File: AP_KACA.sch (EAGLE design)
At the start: 53 parts, among them IC1 REG710XX-3.3, J1 FTDI_DEVICE, M1 WIRELESS-NRF24L01, Q1 BSS123, Q2 BSS123, Q3 BSS123, Q4 BSS123, U2 MPU-6000QFN-24, U3 GY-521MPU6050, Y1 8MHz

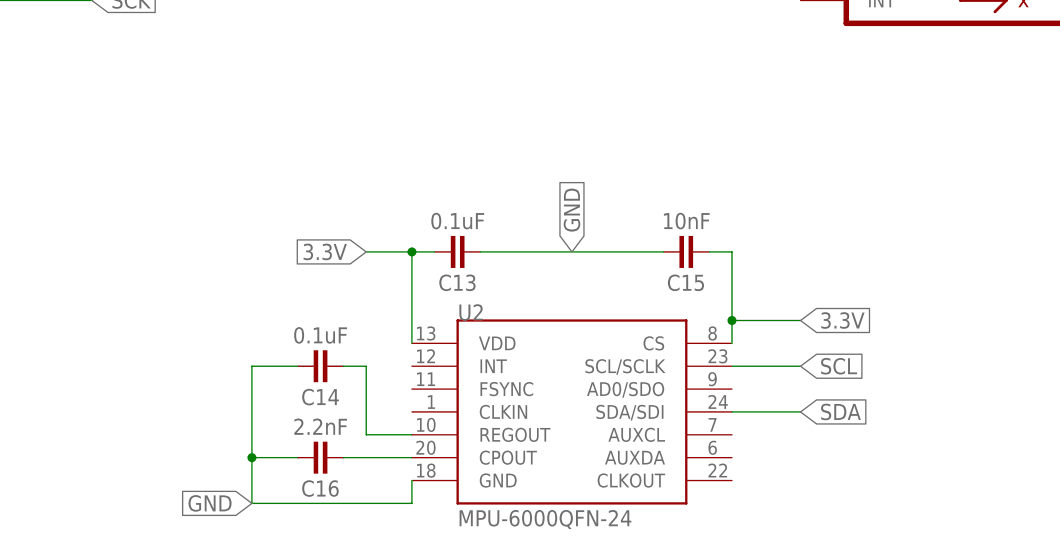
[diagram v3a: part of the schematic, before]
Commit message: removed something
removed the other imu
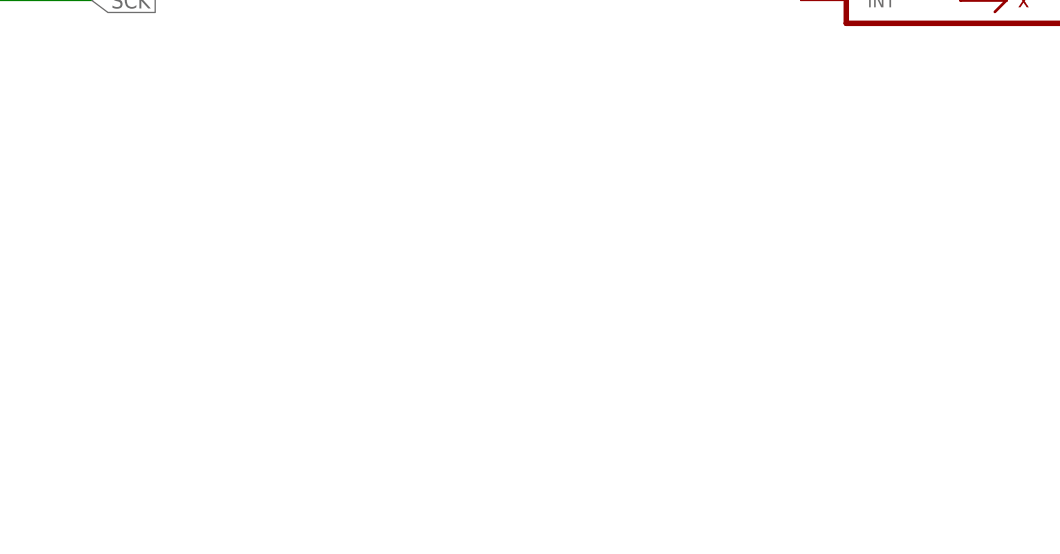
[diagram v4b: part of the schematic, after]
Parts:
- removed C13, C14: 0.1uF, we-rcl:CAPACITOR-1206
- removed C15: 10nF, we-rcl:CAPACITOR-1206
- removed C16: 2.2nF, we-rcl:CAPACITOR-1206
- removed U2: MPU-6000QFN-24, SparkFun-Sensors:MPU-6000QFN-24
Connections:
- removed net N$13: C14.1, U2.REGOUT
- removed net N$14: C16.1, U2.CPOUT
- net 3.3V: no longer C13.2, C15.1, U2.CS, U2.VDD
- net GND: no longer C13.1, C14.2, C15.2, C16.2, U2.GND
- net SCL: no longer U2.SCL/SCLK
- net SDA: no longer U2.SDA/SDI
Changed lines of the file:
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@@
 <layer number="60" name="bCarbon" color="7" fill="1" visible="no" active="no"/>
 <layer number="88" name="SimResults" color="9" fill="1" visible="yes" active="yes"/>
-<layer number="89" name="SimProbes" color="9" fill="1" visible="yes" active="yes"/>
+<layer number="89" name="SimProbes" color="9" fill="1" visible="no" active="yes"/>
 <layer number="90" name="Modules" color="5" fill="1" visible="yes" active="yes"/>
 <layer number="91" name="Nets" color="2" fill="1" visible="yes" active="yes"/>
 <layer number="92" name="Busses" color="1" fill="1" visible="yes" active="yes"/>
-<layer number="93" name="Pins" color="2" fill="1" visible="no" active="yes"/>
+<layer number="93" name="Pins" color="2" fill="1" visible="yes" active="yes"/>
 <layer number="94" name="Symbols" color="4" fill="1" visible="yes" active="yes"/>
 <layer number="95" name="Names" color="7" fill="1" visible="yes" active="yes"/>
@@
 <part name="C11" library="we-rcl" deviceset="CAPACITOR" device="-1206" value="2.2uF"/>
 <part name="C12" library="we-rcl" deviceset="CAPACITOR" device="-1206" value="2.2uF"/>
-<part name="U2" library="SparkFun-Sensors" deviceset="MPU-6000" device="QFN-24"/>
-<part name="C13" library="we-rcl" deviceset="CAPACITOR" device="-1206" value="0.1uF"/>
-<part name="C14" library="we-rcl" deviceset="CAPACITOR" device="-1206" value="0.1uF"/>
-<part name="C15" library="we-rcl" deviceset="CAPACITOR" device="-1206" value="10nF"/>
-<part name="C16" library="we-rcl" deviceset="CAPACITOR" device="-1206" value="2.2nF"/>
 <part name="R3" library="SparkFun-Resistors" deviceset="10.5KOHM1/10W1%(0603)" device="" value="36k"/>
 <part name="Q2" library="transistor-small-signal" library_urn="urn:adsk.eagle:library:401" deviceset="BSS123" device="" package3d_urn="urn:adsk.eagle:package:29752/1"/>
@@
 <instance part="C11" gate="C" x="269.24" y="48.26" rot="R180"/>
 <instance part="C12" gate="C" x="228.6" y="48.26" rot="R180"/>
-<instance part="U2" gate="G$1" x="142.24" y="-27.94"/>
-<instance part="C13" gate="C" x="129.54" y="-10.16" rot="R180"/>
-<instance part="C14" gate="C" x="114.3" y="-22.86" rot="R180"/>
-<instance part="C15" gate="C" x="154.94" y="-10.16" rot="R180"/>
-<instance part="C16" gate="C" x="114.3" y="-33.02" rot="R180"/>
 <instance part="R3" gate="G$1" x="-40.64" y="73.66" rot="R90"/>
 <instance part="Q2" gate="G$1" x="-91.44" y="83.82"/>
@@
 <label x="66.04" y="129.54" size="1.778" layer="95" xref="yes"/>
 </segment>
-<segment>
-<pinref part="U2" gate="G$1" pin="VDD"/>
-<wire x1="124.46" y1="-20.32" x2="124.46" y2="-10.16" width="0.1524" layer="91"/>
-<wire x1="124.46" y1="-10.16" x2="119.38" y2="-10.16" width="0.1524" layer="91"/>
-<label x="119.38" y="-10.16" size="1.778" layer="95" rot="R180" xref="yes"/>
-<wire x1="124.46" y1="-10.16" x2="127" y2="-10.16" width="0.1524" layer="91"/>
-<junction x="124.46" y="-10.16"/>
-<pinref part="C13" gate="C" pin="2"/>
-</segment>
-<segment>
-<pinref part="U2" gate="G$1" pin="CS"/>
-<wire x1="160.02" y1="-20.32" x2="160.02" y2="-17.78" width="0.1524" layer="91"/>
-<wire x1="160.02" y1="-17.78" x2="160.02" y2="-10.16" width="0.1524" layer="91"/>
-<wire x1="160.02" y1="-10.16" x2="157.48" y2="-10.16" width="0.1524" layer="91"/>
-<pinref part="C15" gate="C" pin="1"/>
-<wire x1="160.02" y1="-17.78" x2="167.64" y2="-17.78" width="0.1524" layer="91"/>
-<junction x="160.02" y="-17.78"/>
-<label x="167.64" y="-17.78" size="1.778" layer="95" xref="yes"/>
-</segment>
 </net>
 <net name="GND" class="0">
@@
 </segment>
 <segment>
-<pinref part="U2" gate="G$1" pin="GND"/>
-<wire x1="124.46" y1="-35.56" x2="124.46" y2="-38.1" width="0.1524" layer="91"/>
-<wire x1="124.46" y1="-38.1" x2="106.68" y2="-38.1" width="0.1524" layer="91"/>
-<label x="106.68" y="-38.1" size="1.778" layer="95" rot="R180" xref="yes"/>
-<pinref part="C14" gate="C" pin="2"/>
-<wire x1="111.76" y1="-22.86" x2="106.68" y2="-22.86" width="0.1524" layer="91"/>
-<wire x1="106.68" y1="-22.86" x2="106.68" y2="-33.02" width="0.1524" layer="91"/>
-<pinref part="C16" gate="C" pin="2"/>
-<wire x1="106.68" y1="-33.02" x2="106.68" y2="-38.1" width="0.1524" layer="91"/>
-<wire x1="111.76" y1="-33.02" x2="106.68" y2="-33.02" width="0.1524" layer="91"/>
-<junction x="106.68" y="-33.02"/>
-</segment>
-<segment>
-<pinref part="C13" gate="C" pin="1"/>
-<wire x1="132.08" y1="-10.16" x2="152.4" y2="-10.16" width="0.1524" layer="91"/>
-<label x="142.24" y="-10.16" size="1.778" layer="95" rot="R90" xref="yes"/>
-<pinref part="C15" gate="C" pin="2"/>
-</segment>
-<segment>
 <pinref part="R7" gate="G$1" pin="2"/>
 <wire x1="60.96" y1="10.16" x2="66.04" y2="10.16" width="0.1524" layer="91"/>
@@
 <label x="162.56" y="38.1" size="1.778" layer="95" rot="R180" xref="yes"/>
 </segment>
-<segment>
-<pinref part="U2" gate="G$1" pin="SDA/SDI"/>
-<wire x1="160.02" y1="-27.94" x2="167.64" y2="-27.94" width="0.1524" layer="91"/>
-<label x="167.64" y="-27.94" size="1.778" layer="95" xref="yes"/>
-</segment>
 </net>
 <net name="SCL" class="0">
@@
 <wire x1="167.64" y1="43.18" x2="162.56" y2="43.18" width="0.1524" layer="91"/>
 <label x="162.56" y="43.18" size="1.778" layer="95" rot="R180" xref="yes"/>
-</segment>
-<segment>
-<pinref part="U2" gate="G$1" pin="SCL/SCLK"/>
-<wire x1="160.02" y1="-22.86" x2="167.64" y2="-22.86" width="0.1524" layer="91"/>
-<label x="167.64" y="-22.86" size="1.778" layer="95" xref="yes"/>
 </segment>
 </net>
@@
 </segment>
 </net>
-<net name="N$14" class="0">
-<segment>
-<pinref part="U2" gate="G$1" pin="CPOUT"/>
-<wire x1="124.46" y1="-33.02" x2="116.84" y2="-33.02" width="0.1524" layer="91"/>
-<pinref part="C16" gate="C" pin="1"/>
-</segment>
-</net>
-<net name="N$13" class="0">
-<segment>
-<pinref part="C14" gate="C" pin="1"/>
-<wire x1="116.84" y1="-22.86" x2="119.38" y2="-22.86" width="0.1524" layer="91"/>
-<wire x1="119.38" y1="-22.86" x2="119.38" y2="-30.48" width="0.1524" layer="91"/>
-<pinref part="U2" gate="G$1" pin="REGOUT"/>
-<wire x1="119.38" y1="-30.48" x2="124.46" y2="-30.48" width="0.1524" layer="91"/>
-</segment>
-</net>
